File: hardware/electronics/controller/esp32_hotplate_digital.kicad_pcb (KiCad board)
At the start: 2 copper layers, 89.1 x 49.4 mm, 92 parts, among them IC1 ADC081S021CIMF_NOPB, IC2 ADC081S021CIMF_NOPB, J1 USB_C_Receptacle_USB2.0, J2 JST XH, J3 JST XH, J4 JST XH, J5 JST XH, J7 JST XH, J8 105162-0001, J9 Conn_01x04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

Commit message: finalized the controller version 2
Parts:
- added D10: LED, LED_SMD:LED_0805_2012Metric_Pad1.15x1.40mm_HandSolder, F.Cu at (87.9, 97.6)
- added D5: LED, LED_SMD:LED_0805_2012Metric_Pad1.15x1.40mm_HandSolder, F.Cu at (85.9, 97.6)
- added R28: 10k, Resistor_SMD:R_0805_2012Metric_Pad1.20x1.40mm_HandSolder, F.Cu at (82.9, 98.5)
- added R29: 10k, Resistor_SMD:R_0805_2012Metric_Pad1.20x1.40mm_HandSolder, F.Cu at (82.9, 96.5)
- D8: moved to F.Cu
- R20: value R -> 10k; moved to F.Cu
- R5, R6: value 10k -> 5.1k
- R7, R8: value R -> 10k
- R9: value R -> 4k7
- moved C19 35.4 mm to (80.6, 94.3), turned to 90 degrees
- moved R19 33.3 mm to (82.7, 94.3), turned to -90 degrees
- moved R10 19.4 mm to (123.0, 97.4), turned to 135 degrees
- moved D8 17.6 mm to (90.0, 97.6), turned to 90 degrees
- moved R20 14.0 mm to (92.0, 97.6)
- moved R21 2.44 mm to (122.0, 72.5), turned to 0 degrees
- moved R22 2.08 mm to (122.0, 75.5), turned to 0 degrees
- moved J8 1.60 mm to (122.7, 86.3)
- moved R27 1.60 mm to (112.0, 94.7)
- moved R26 1.60 mm to (113.4, 93.3)
- moved R25 1.49 mm to (116.0, 95.5)
- moved R23 1.36 mm to (109.1, 72.3)
- moved R24 1.36 mm to (111.3, 73.5)
- moved R12 0.82 mm to (94.3, 64.2), turned to 45 degrees
- moved R6 0.59 mm to (51.1, 55.2)
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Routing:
- net /HEATER: track 41.9 -> 80.8 mm, vias 4 -> 3
- net Net-(R10-Pad2): track 66.1 -> 39.5 mm
- net /HSPI_MISO: track 79.7 -> 105.5 mm, vias 0 -> 1
- net /SD_CS: track 68.1 -> 85.8 mm
- net /HSPI_MOSI: track 70.2 -> 86.1 mm
- net /FAN: track 36.5 -> 50.4 mm, vias 4 -> 2
- net /HSPI_CLK: track 84.6 -> 96.9 mm, vias 2 -> 1
- net GND: track 113.2 -> 101.1 mm
- net /BTN_SELECT: track 72.8 -> 66.2 mm
- net Net-(D10-A): track 0.00 -> 5.54 mm
- net /GPIO_0: track 28.5 -> 34.0 mm
- net /EN: track 53.5 -> 58.9 mm
- net +12V: track 80.9 -> 84.6 mm
- net /VSPI_MOSI: track 28.2 -> 31.9 mm
- net /BUZZER: track 23.3 -> 26.9 mm
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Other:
- board text added: "12V0"
- board text added: "3V3"
- board text added: "5V0"

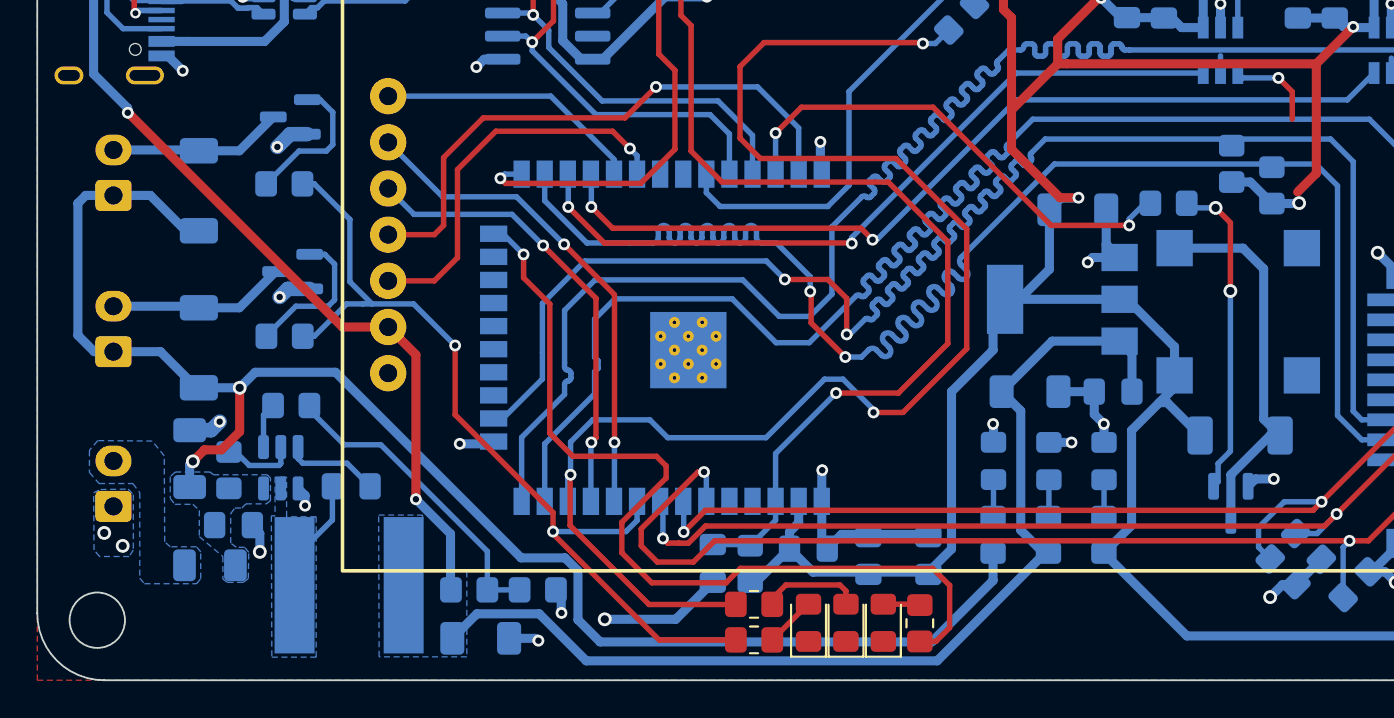
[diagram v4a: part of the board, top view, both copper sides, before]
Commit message: redraw polygons with 45* angles
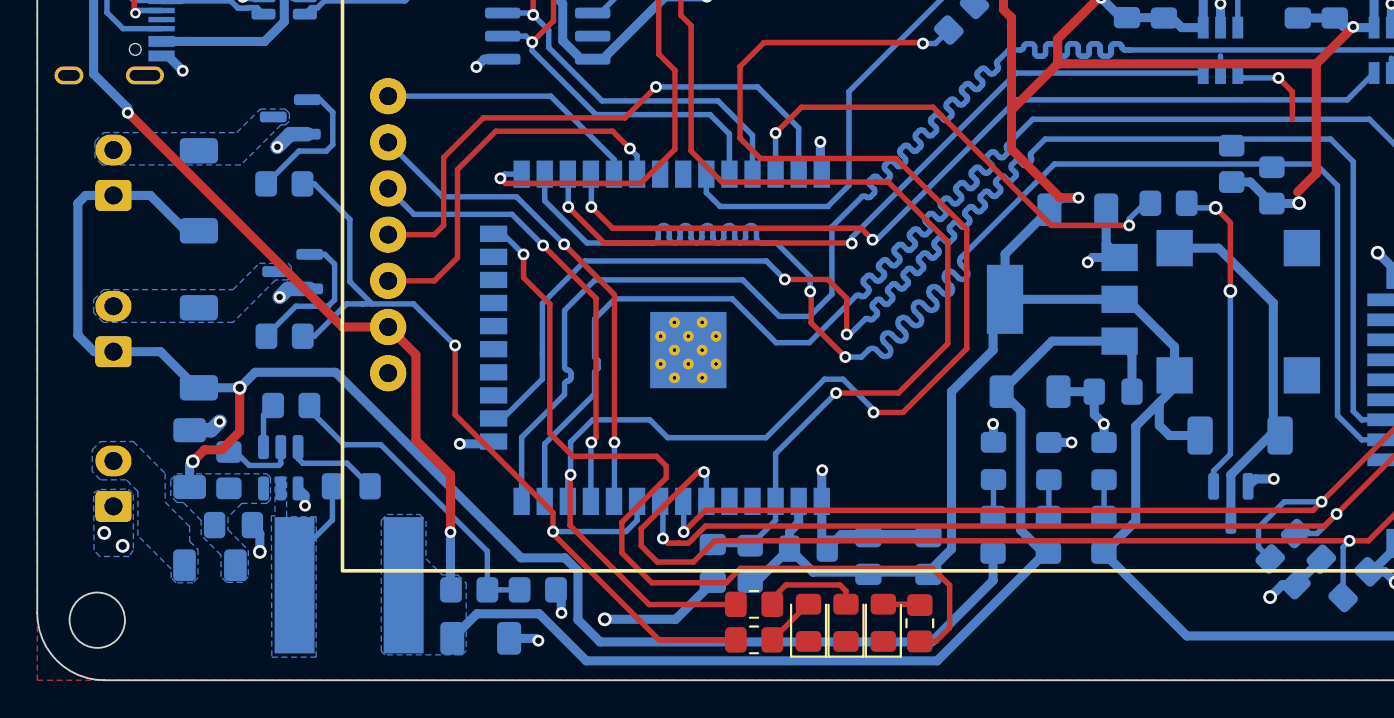
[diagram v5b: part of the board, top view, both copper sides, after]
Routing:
- net Net-(D7-A): track 9.78 -> 0.00 mm
- net Net-(D6-A): track 9.58 -> 0.00 mm
- net Net-(BZ1-+): track 21.0 -> 20.2 mm
- added copper zone on B.Cu, net Net-(D6-A)
- added copper zone on B.Cu, net Net-(D7-A)

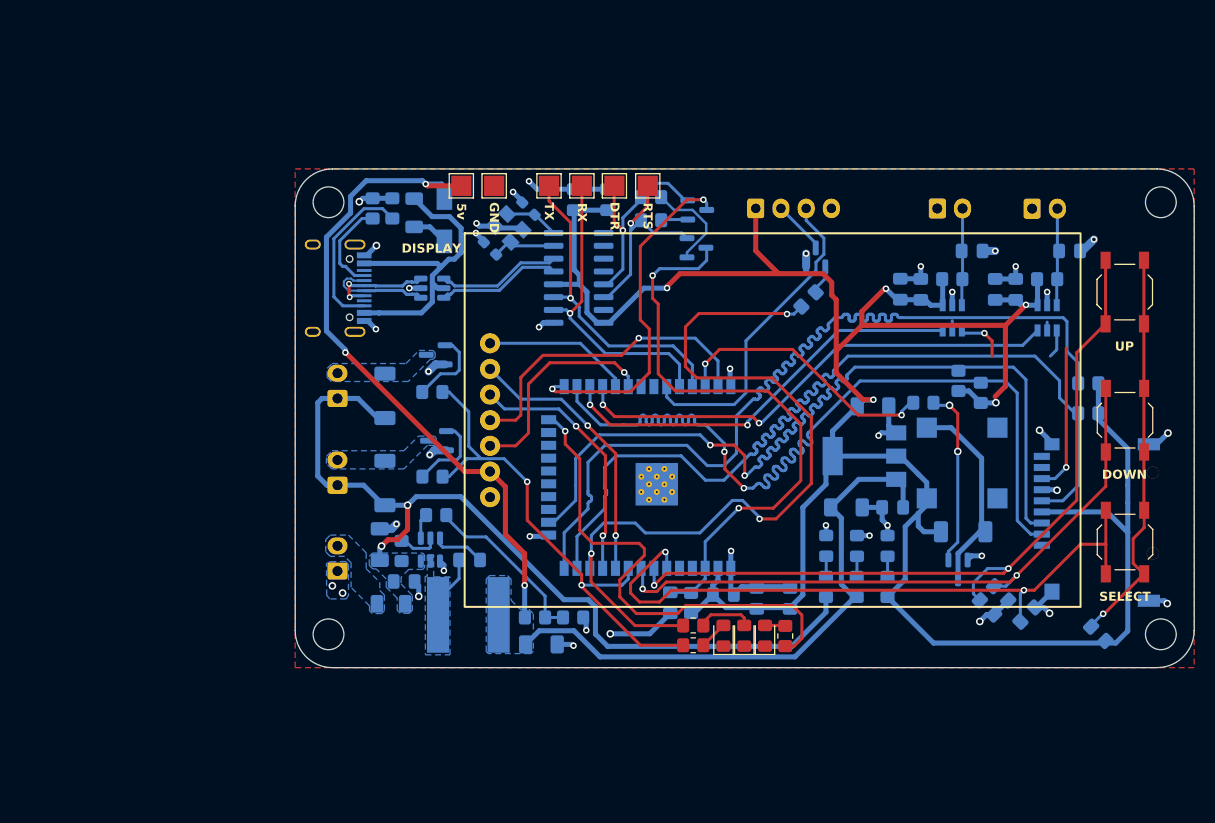
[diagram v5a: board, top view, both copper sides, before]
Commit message: updated code + added 3d pintable parts + added thermal isolation pcb
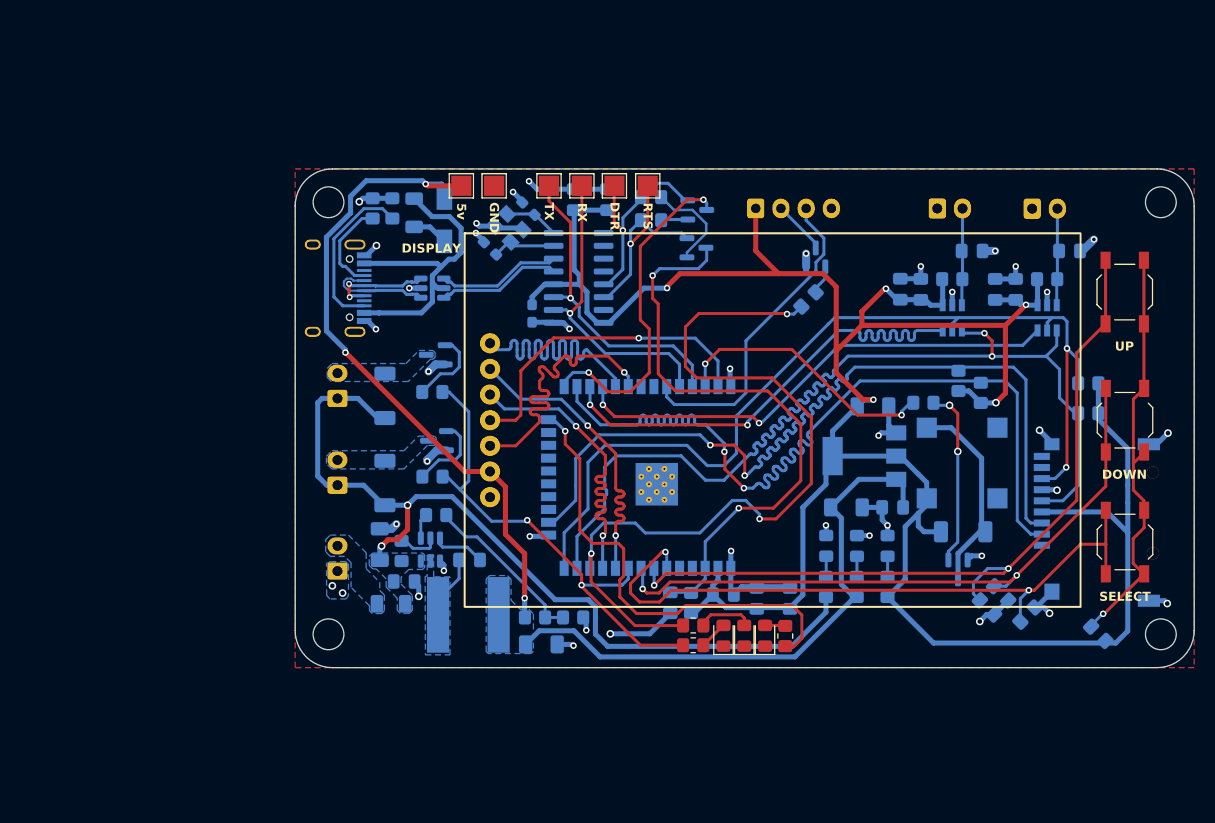
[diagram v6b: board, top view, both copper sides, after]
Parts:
- added C22: 0.1uf, Capacitor_SMD:C_0603_1608Metric_Pad1.08x0.95mm_HandSolder, B.Cu at (66.9, 65.6)
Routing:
- net /VSPI_CS: track 14.9 -> 33.5 mm
- net /HSPI_MISO: track 105.5 -> 93.1 mm, vias 1 -> 2
- net /VSPI_CLK: track 21.8 -> 32.0 mm
- net /ADC1_CS: track 41.4 -> 48.6 mm
- net /DISP_RST: track 25.2 -> 30.5 mm
- net +3.3V: track 243.8 -> 247.8 mm
- net /DISP_DC: track 27.5 -> 30.6 mm
- net /STATUS: track 49.2 -> 46.3 mm
- net /RTS: track 19.8 -> 22.4 mm
- net Net-(R10-Pad2): track 39.5 -> 41.9 mm
- net GND: track 101.1 -> 103.3 mm
- net /FAN: track 50.4 -> 48.9 mm
- net Net-(R2-Pad2): track 17.7 -> 16.6 mm
- net /GPIO_0: track 34.0 -> 33.1 mm
- net /HSPI_CLK: track 96.9 -> 97.7 mm, vias 1 -> 2
